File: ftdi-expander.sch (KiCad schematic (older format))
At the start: 17 parts, among them J1 Conn_01x10, J2 Conn_01x10, J3 ARM-JTAG-10, J4 IDC 02x04, J5 AVR-ISP-6, J6 Conn_01x06_Male, SW1 SW_SPDT, SW2 SW_SPDT, U1 AZ1117EH-3.3TRG1

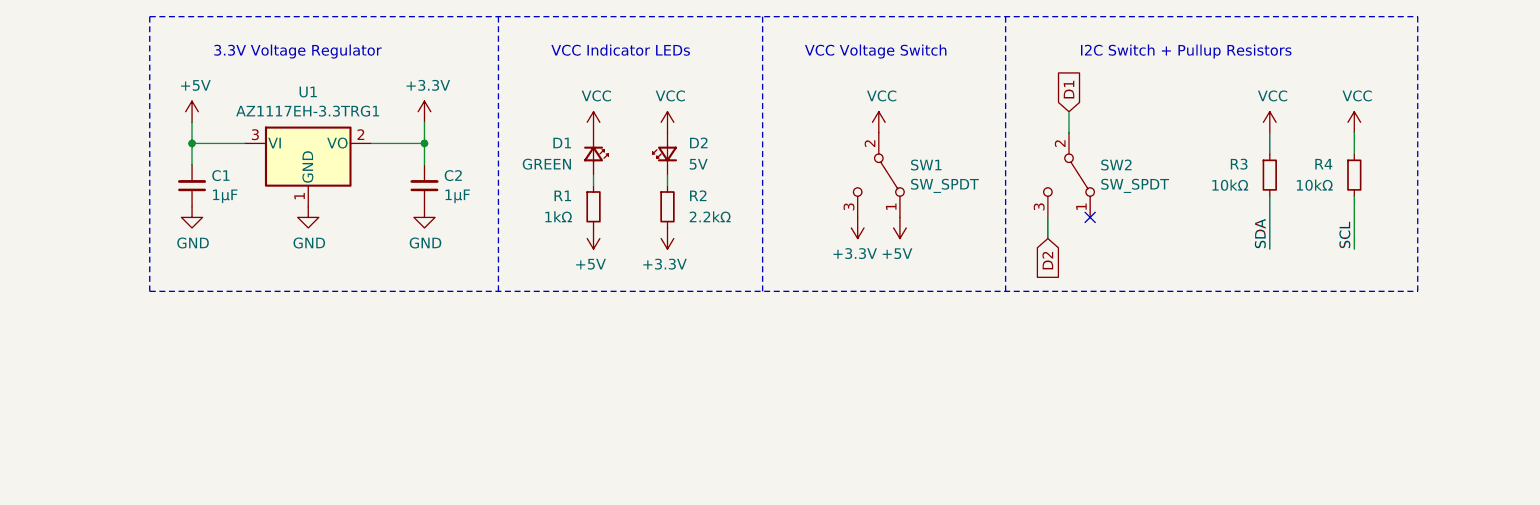
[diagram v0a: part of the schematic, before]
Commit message: routed version with spdt switches
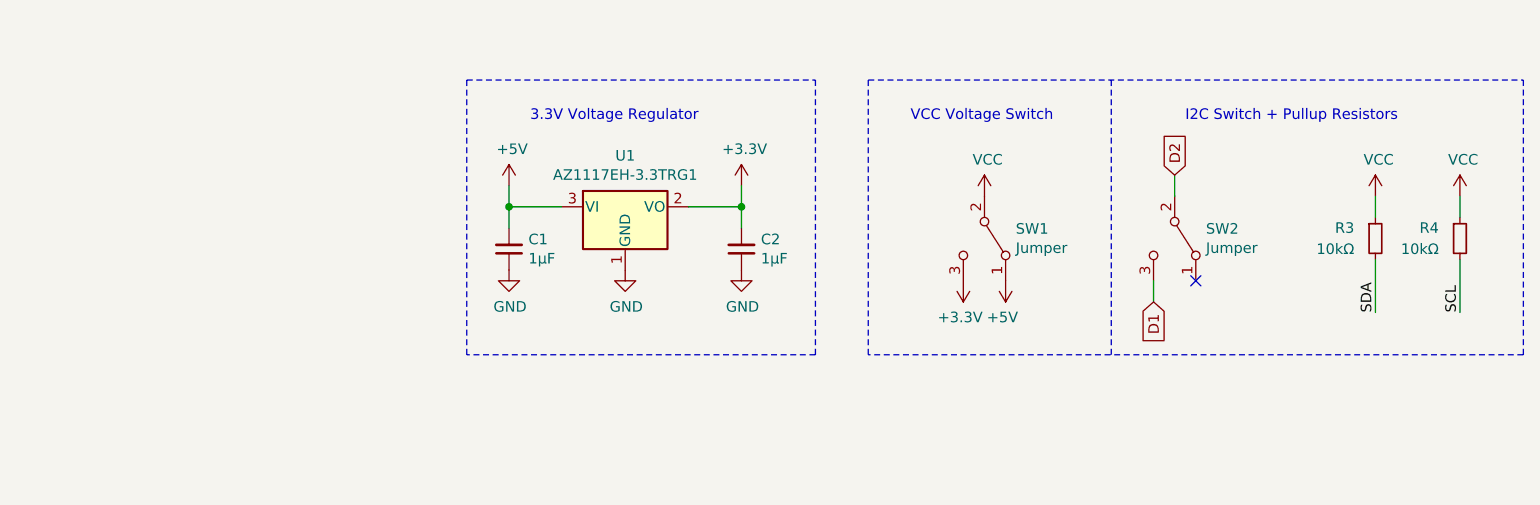
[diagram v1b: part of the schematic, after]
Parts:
- removed D1: GREEN, LED_SMD:LED_0805_2012Metric_Castellated, symbol Device:LED_Small
- removed D2: 5V, LED_SMD:LED_0805_2012Metric_Castellated, symbol Device:LED_Small
- removed R1: 1kΩ, Resistor_SMD:R_0805_2012Metric_Pad1.15x1.40mm_HandSolder, symbol Device:R_Small
- removed R2: 2.2kΩ, Resistor_SMD:R_0805_2012Metric_Pad1.15x1.40mm_HandSolder, symbol Device:R_Small
- SW1, SW2: value SW_SPDT -> Jumper; footprint Button_Switch_SMD:SW_SPDT_PCM12 -> Connector_PinHeader_2.54mm:PinHeader_1x03_P2.54mm_Vertical
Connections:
- net D1: now also SW2.3 (C); no longer SW2.2 (B)
- net D2: now also SW2.2 (B); no longer SW2.3 (C)
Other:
- note removed: "VCC Indicator LEDs"
- moved on the sheet: C1, C2, R3, R4, SW1, SW2, U1
